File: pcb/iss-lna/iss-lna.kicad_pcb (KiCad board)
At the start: 2 copper layers, 40 parts, among them J1 SMA, J2 UFL, J3 UFL, J4 SMA, J5 UFL, J6 UFL, Q1 BFU520R

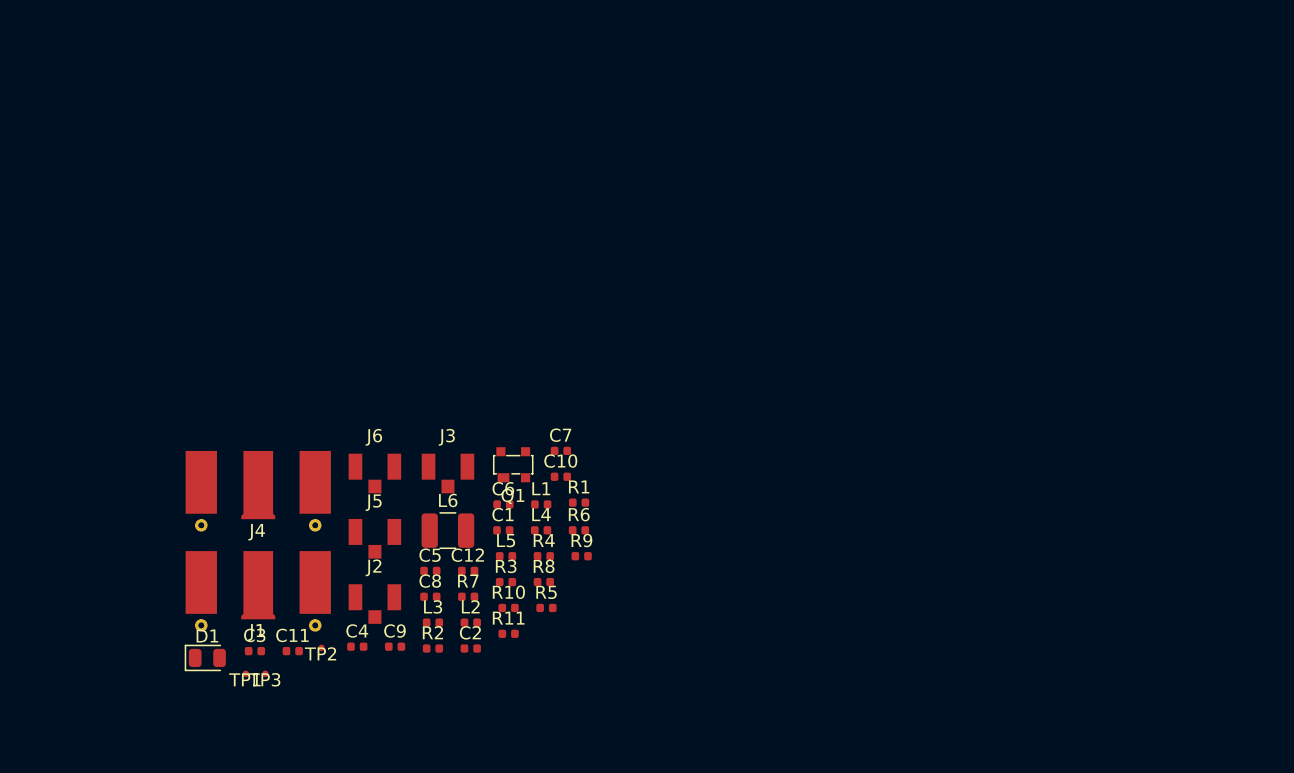
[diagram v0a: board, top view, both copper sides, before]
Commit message: Layout almost done TODO silkscreen cleanup TODO via stitching
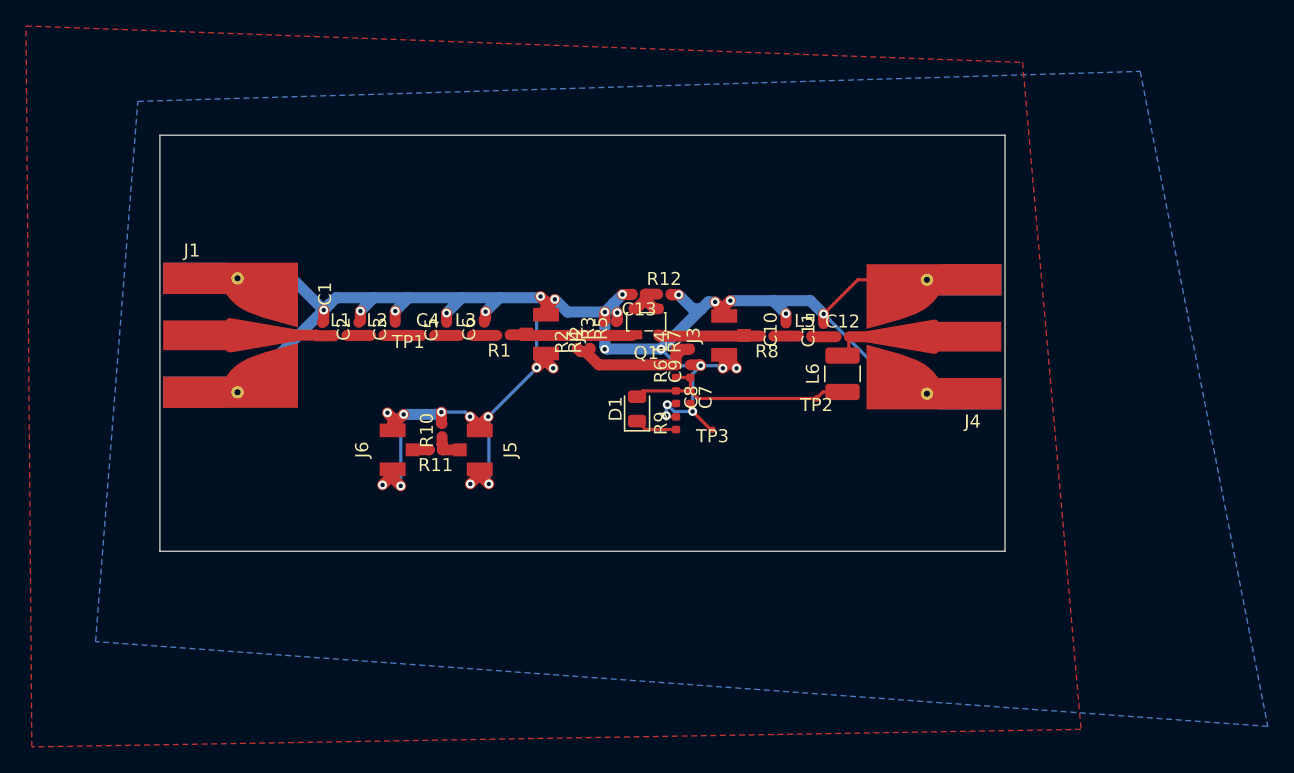
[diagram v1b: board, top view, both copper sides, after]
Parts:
- added C13: 470 pF, Capacitor_SMD:C_0402_1005Metric, F.Cu at (115.8, 54.2)
- added R12: 0R, Resistor_SMD:R_0402_1005Metric, F.Cu at (117.8, 54.2)
- J1, J4: footprint iss_lna:142-0701-801 -> iss_lna:142-0701-801-with-taper
- moved J4 58.0 mm to (144.0, 57.5), turned to 270 degrees
- moved C11 47.7 mm to (130.1, 57.0), turned to 90 degrees
- moved TP2 42.6 mm to (129.5, 62.2)
- moved TP3 39.2 mm to (121.5, 64.7)
- moved D1 38.2 mm to (115.7, 63.0), turned to 90 degrees
- moved C12 34.0 mm to (131.5, 57.5)
- moved L6 32.7 mm to (131.5, 60.4), turned to 90 degrees
- moved C9 31.1 mm to (119.8, 60.1), turned to 90 degrees
- moved TP1 28.9 mm to (98.1, 57.4)
- moved L5 28.5 mm to (128.6, 57.5)
- moved C3 27.0 mm to (97.1, 56.9), turned to 90 degrees
- moved R2 26.1 mm to (111.1, 57.9), turned to 90 degrees
- moved C2 26.0 mm to (94.3, 56.9), turned to 90 degrees
- moved R7 26.0 mm to (119.8, 57.9), turned to 90 degrees
- moved R8 25.5 mm to (125.7, 57.5), turned to 180 degrees
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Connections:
- net Net-(C7-Pad1) renamed /VCC
- Q1 pad 3: GND -> Net-(C13-Pad1)
- Q1 pad 4: GND -> Net-(C13-Pad1)
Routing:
- net GND: track 0.00 -> 178.9 mm, vias 0 -> 34
- net /VCC: track 0.00 -> 18.6 mm
- net Net-(C12-Pad2): track 0.00 -> 12.3 mm
- net Net-(L4-Pad1): track 0.00 -> 11.0 mm
- net Net-(J2-Pad1): track 0.00 -> 9.61 mm
- net Net-(C1-Pad1): track 0.00 -> 9.53 mm
- net Net-(J3-Pad1): track 0.00 -> 7.89 mm
- net Net-(C13-Pad1): track 0.00 -> 3.86 mm
- net Net-(D1-Pad1): track 0.00 -> 3.27 mm
- net Net-(C3-Pad1): track 0.00 -> 2.89 mm
- net Net-(J5-Pad1): track 0.00 -> 2.38 mm
- net Net-(C11-Pad1): track 0.00 -> 1.91 mm
- net Net-(C10-Pad1): track 0.00 -> 1.91 mm
- net Net-(C6-Pad1): track 0.00 -> 1.89 mm
- net Net-(C4-Pad2): track 0.00 -> 1.89 mm
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- added copper zone on B.Cu, net GND
- added copper zone on F.Cu, net GND
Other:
- board outline added: 65 x 32 mm
- net class Default: clearance 0.2 -> 0.16; trace_width 0.25 -> 0.16; via_dia 0.8 -> 0.69; via_drill 0.4 -> 0.33
- net class RF1 added: clearance 0.16, trace_width 0.849, via_dia 0.69, via_drill 0.33
- rule trace_clearance: 0.2 -> 0.16
- rule trace_min: 0.2 -> 0.16

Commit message: Fix silkscreen, add mounting holes, generate Gerbers
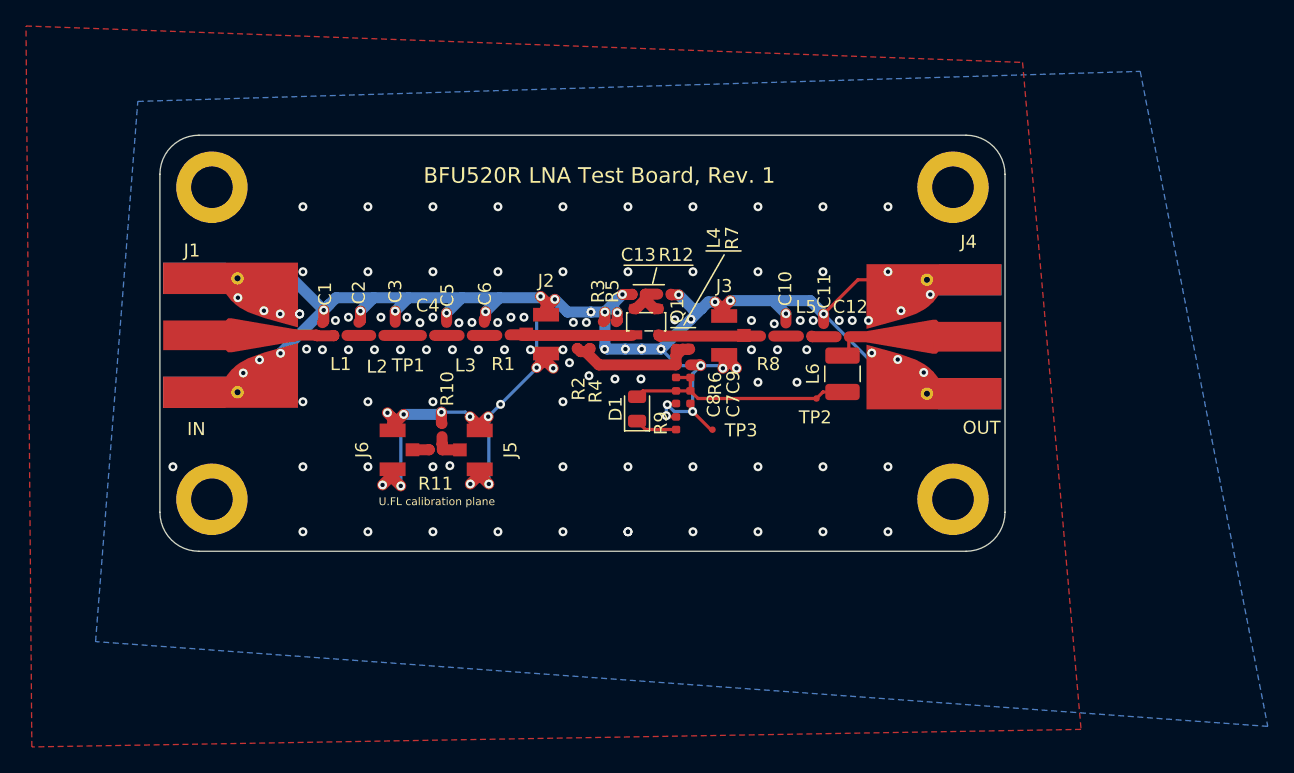
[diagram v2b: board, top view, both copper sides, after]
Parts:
- added H1: MountingHole_Pad, MountingHole:MountingHole_3.2mm_M3_ISO14580_Pad, F.Cu at (83.0, 46.0)
- added H2: MountingHole_Pad, MountingHole:MountingHole_3.2mm_M3_ISO14580_Pad, F.Cu at (83.0, 70.0)
- added H3: MountingHole_Pad, MountingHole:MountingHole_3.2mm_M3_ISO14580_Pad, F.Cu at (140.0, 46.0)
- added H4: MountingHole_Pad, MountingHole:MountingHole_3.2mm_M3_ISO14580_Pad, F.Cu at (140.0, 70.0)
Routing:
- net GND: vias 34 -> 139
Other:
- outline, holes or cut-outs redrawn
- board text added: "BFU520R LNA Test Board, Rev. 1"
- board text added: "IN"
- board text added: "OUT"
- board text added: "U.FL calibration plane"

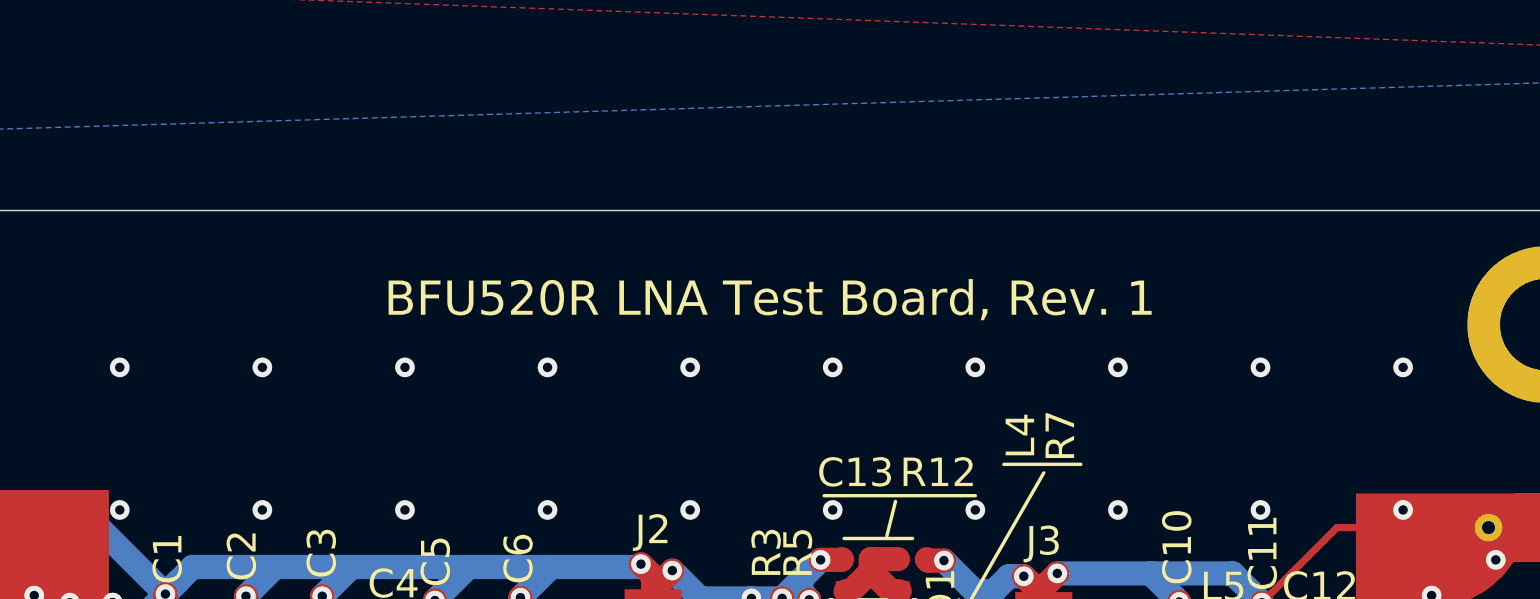
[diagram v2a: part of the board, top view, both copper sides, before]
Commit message: Rename to amplifier board
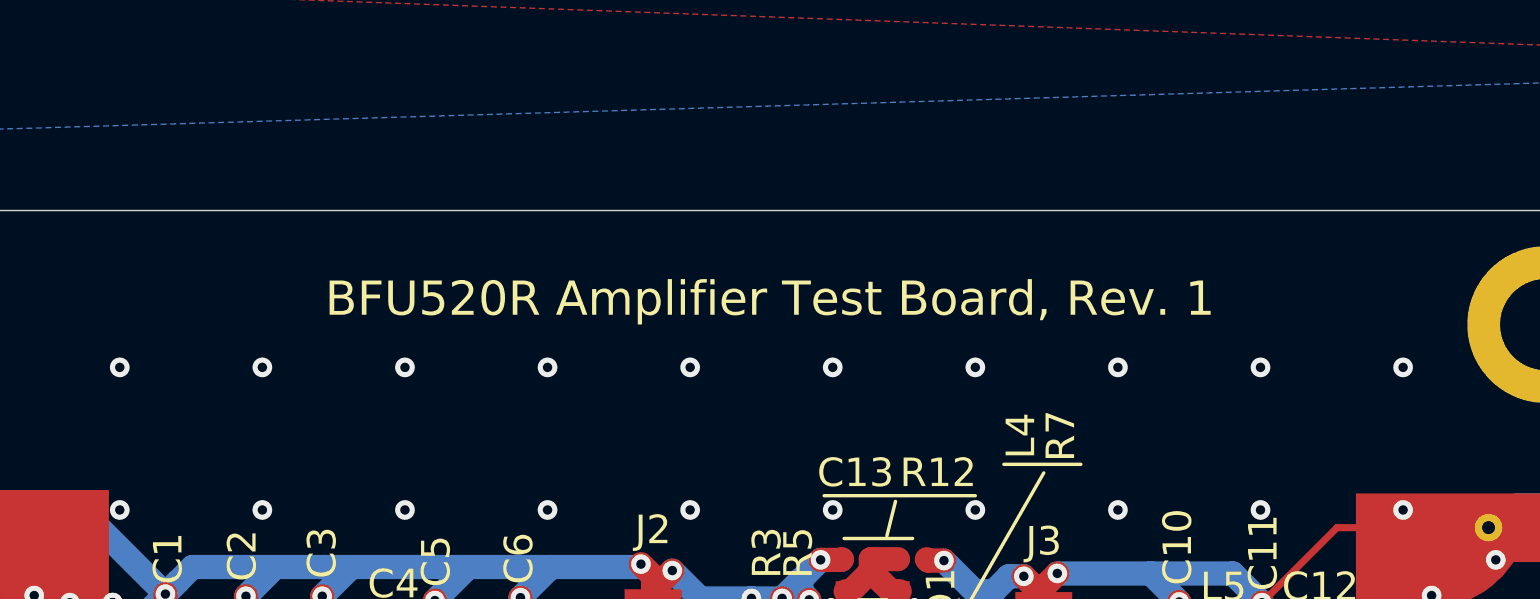
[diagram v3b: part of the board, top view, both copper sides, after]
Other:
- board text added: "BFU520R Amplifier Test Board, Rev. 1"
- board text removed: "BFU520R LNA Test Board, Rev. 1"
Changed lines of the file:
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@@
     (effects (font (size 0.6 0.6) (thickness 0.1)))
   )
-  (gr_text "BFU520R LNA Test Board, Rev. 1" (at 112.8 45.1) (layer F.SilkS)
+  (gr_text "BFU520R Amplifier Test Board, Rev. 1" (at 112.8 45.1) (layer F.SilkS)
     (effects (font (size 1.2 1.2) (thickness 0.15)))
   )
